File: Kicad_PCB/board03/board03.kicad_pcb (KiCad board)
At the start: 2 copper layers, 42 x 20 mm, 7 parts, among them J1 USB_B_Micro, Q1 BF545C, U1 STM32F401CCFx, U2 AMS1117-3.3, U3 tmag5273

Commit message: coil and all
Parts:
- added L1: L_core_v, L_Core_vlv:L_core_v, B.Cu at (168.0, 98.0)
- moved Q1 2.50 mm to (168.0, 97.0)
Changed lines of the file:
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@@
     (tracks 0)
     (zones 0)
-    (modules 7)
-    (nets 72)
+    (modules 8)
+    (nets 74)
   )
   (page A4)
@@
   (net 70 "Net-(D2-Pad2)")
   (net 71 "Net-(D2-Pad1)")
+  (net 72 "Net-(L1-Pad2)")
+  (net 73 "Net-(L1-Pad1)")
   (net_class Default "This is the default net class."
     (clearance 0.2)
@@
     (add_net "Net-(J1-Pad5)")
     (add_net "Net-(J1-Pad6)")
+    (add_net "Net-(L1-Pad1)")
+    (add_net "Net-(L1-Pad2)")
     (add_net "Net-(Q1-Pad1)")
     (add_net "Net-(Q1-Pad2)")
@@
     (add_net "Net-(U3-Pad6)")
   )
+  (module L_Core_vlv:L_core_v (layer B.Cu)
+    (at 168 98)
+    (fp_text reference L1 (at -3.5 1.5) (layer B.SilkS)
+      (effects (font (size 1 1) (thickness 0.15)) (justify mirror))
+    )
+    (fp_text value L_core_v (at -1 3) (layer B.Fab)
+      (effects (font (size 0.7 0.5) (thickness 0.125)) (justify mirror))
+    )
+    (pad 2 smd rect (at 1.5 1.5) (size 2 1.5) (layers B.Cu B.Paste B.Mask)
+      (net 72 "Net-(L1-Pad2)"))
+    (pad 1 smd rect (at -1.5 1.5) (size 2 1.5) (layers B.Cu B.Paste B.Mask)
+      (net 73 "Net-(L1-Pad1)"))
+  )
   (module LED_SMD:LED_0805_2012Metric (layer F.Cu)
     (at 165.0625 107)
@@
   )
   (module Package_TO_SOT_SMD:SOT-23 (layer F.Cu)
-    (at 168 99.5)
+    (at 168 97)
     (descr "SOT-23, Standard")
     (tags SOT-23)
     (attr smd)
-    (fp_text reference Q1 (at 0 -2.5) (layer F.SilkS)
+    (fp_text reference Q1 (at -3 0) (layer F.SilkS)
       (effects (font (size 1 1) (thickness 0.15)))
     )
-    (fp_text value BF545C (at 0 2.5) (layer F.Fab)
+    (fp_text value BF545C (at 2.5 0 90) (layer F.Fab)
       (effects (font (size 0.7 0.5) (thickness 0.1)))
     )

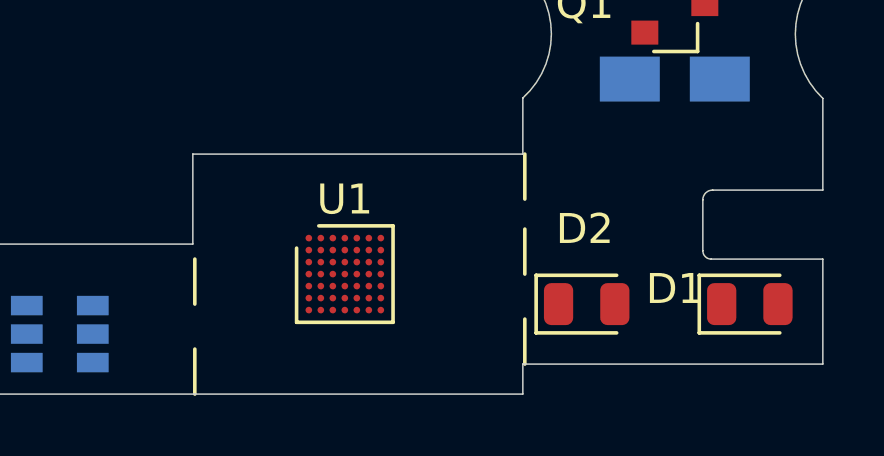
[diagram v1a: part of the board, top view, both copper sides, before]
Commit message: cap toch sensor
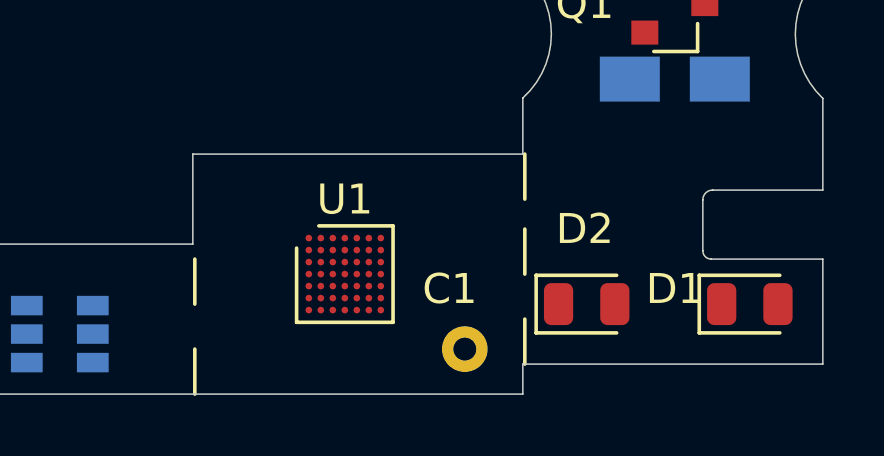
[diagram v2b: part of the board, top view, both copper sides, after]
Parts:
- added C1: captouch, cap_touch:capS, F.Cu at (161.0, 109.0)
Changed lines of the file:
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@@
     (tracks 0)
     (zones 0)
-    (modules 8)
-    (nets 74)
+    (modules 9)
+    (nets 75)
   )
   (page A4)
@@
   (net 72 "Net-(L1-Pad2)")
   (net 73 "Net-(L1-Pad1)")
+  (net 74 "Net-(C1-Pad1)")
   (net_class Default "This is the default net class."
     (clearance 0.2)
@@
     (uvia_dia 0.3)
     (uvia_drill 0.1)
+    (add_net "Net-(C1-Pad1)")
     (add_net "Net-(D1-Pad1)")
     (add_net "Net-(D1-Pad2)")
@@
     (add_net "Net-(U3-Pad6)")
   )
+  (module cap_touch:capS (layer F.Cu)
+    (at 161 109)
+    (fp_text reference C1 (at -0.5 -2.5) (layer F.SilkS)
+      (effects (font (size 1 1) (thickness 0.15)))
+    )
+    (fp_text value captouch (at 1 -2 90) (layer F.Fab)
+      (effects (font (size 0.5 0.5) (thickness 0.1)))
+    )
+    (pad 1 thru_hole circle (at 0 -0.5) (size 1.524 1.524) (drill 0.762) (layers *.Cu *.Mask)
+      (net 74 "Net-(C1-Pad1)"))
+  )
   (module L_Core_vlv:L_core_v (layer B.Cu)
     (at 168 98)
@@
       (effects (font (size 1 1) (thickness 0.15)))
     )
-    (fp_text value STM32F401CCFx (at 0 2.4825) (layer F.Fab)
+    (fp_text value STM32F401CCFx (at -1 3) (layer F.Fab)
       (effects (font (size 1 0.6) (thickness 0.15)))
     )

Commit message: sensor Vlt
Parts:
- added U4: sensV, sensorVlt:SensV, F.Cu at (156.0, 111.0)
- moved D1 6.75 mm to (165.1, 103.0)
- moved U1 1.58 mm to (155.5, 105.5)
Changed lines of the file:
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@@
     (tracks 0)
     (zones 0)
-    (modules 9)
-    (nets 75)
+    (modules 10)
+    (nets 77)
   )
   (page A4)
@@
   (net 73 "Net-(L1-Pad1)")
   (net 74 "Net-(C1-Pad1)")
+  (net 75 "Net-(U4-Pad2)")
+  (net 76 "Net-(U4-Pad1)")
   (net_class Default "This is the default net class."
     (clearance 0.2)
@@
     (add_net "Net-(U3-Pad5)")
     (add_net "Net-(U3-Pad6)")
+    (add_net "Net-(U4-Pad1)")
+    (add_net "Net-(U4-Pad2)")
+  )
+  (module sensorVlt:SensV (layer F.Cu)
+    (at 156 111)
+    (fp_text reference U4 (at 0 -1.5) (layer F.SilkS)
+      (effects (font (size 1 1) (thickness 0.15)))
+    )
+    (fp_text value sensV (at 0 -4.5) (layer F.Fab)
+      (effects (font (size 1 1) (thickness 0.15)))
+    )
+    (pad 2 smd rect (at 2 -2) (size 1.524 1.524) (layers F.Cu F.Paste F.Mask)
+      (net 75 "Net-(U4-Pad2)"))
+    (pad 1 smd rect (at -2 -2) (size 1.524 1.524) (layers F.Cu F.Paste F.Mask)
+      (net 76 "Net-(U4-Pad1)"))
   )
   (module cap_touch:capS (layer F.Cu)
@@
     (tags diode)
     (attr smd)
-    (fp_text reference D2 (at -0.0625 -2.5) (layer F.SilkS)
+    (fp_text reference D2 (at 2.9375 0) (layer F.SilkS)
       (effects (font (size 1 1) (thickness 0.15)))
     )
@@
   )
   (module LED_SMD:LED_0805_2012Metric (layer F.Cu)
-    (at 170.5 107)
+    (at 165.0625 103)
     (descr "LED SMD 0805 (2012 Metric), square (rectangular) end terminal, IPC_7351 nominal, (Body size source: https://docs.google.com/spreadsheets/d/1BsfQQcO9C6DZCsRaXUlFlo91Tg2WpOkGARC1WS5S8t0/edit?usp=sharing), generated with kicad-footprint-generator")
     (tags diode)
     (attr smd)
-    (fp_text reference D1 (at -2.5 -0.5) (layer F.SilkS)
-      (effects (font (size 1 1) (thickness 0.15)))
-    )
-    (fp_text value LH_R974-LP-1 (at -0.5 1.5) (layer F.Fab)
+    (fp_text reference D1 (at 2.9375 0.5) (layer F.SilkS)
+      (effects (font (size 1 1) (thickness 0.15)))
+    )
+    (fp_text value LH_R974-LP-1 (at 4.4375 -0.5) (layer F.Fab)
       (effects (font (size 0.5 0.5) (thickness 0.1)))
     )
@@
   )
   (module Package_CSP:ST_WLCSP-49_Die423 (layer F.Cu)
-    (at 157 106)
+    (at 155.5 105.5)
     (descr "WLCSP-49, 7x7 raster, 2.965x2.965mm package, pitch 0.4mm; see section 7.1 of http://www.st.com/resource/en/datasheet/stm32f401vc.pdf")
     (tags "BGA 49 0.4")
     (attr smd)
-    (fp_text reference U1 (at 0 -2.4825) (layer F.SilkS)
-      (effects (font (size 1 1) (thickness 0.15)))
-    )
-    (fp_text value STM32F401CCFx (at -1 3) (layer F.Fab)
-      (effects (font (size 1 0.6) (thickness 0.15)))
+    (fp_text reference U1 (at 3.5 -1.5) (layer F.SilkS)
+      (effects (font (size 1 1) (thickness 0.15)))
+    )
+    (fp_text value STM32F401CCFx (at 0.5 -3) (layer F.Fab)
+      (effects (font (size 0.6 0.6) (thickness 0.1)))
     )
     (fp_text user %R (at 0 0) (layer F.Fab)
